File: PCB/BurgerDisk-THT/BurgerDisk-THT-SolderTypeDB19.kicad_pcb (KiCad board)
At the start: 2 copper layers, 93.7 x 67.6 mm, 18 parts, among them J1 Daisy port in, J2 MicroSD module, J3 UART, J4 Daisy port out, U1 PC817

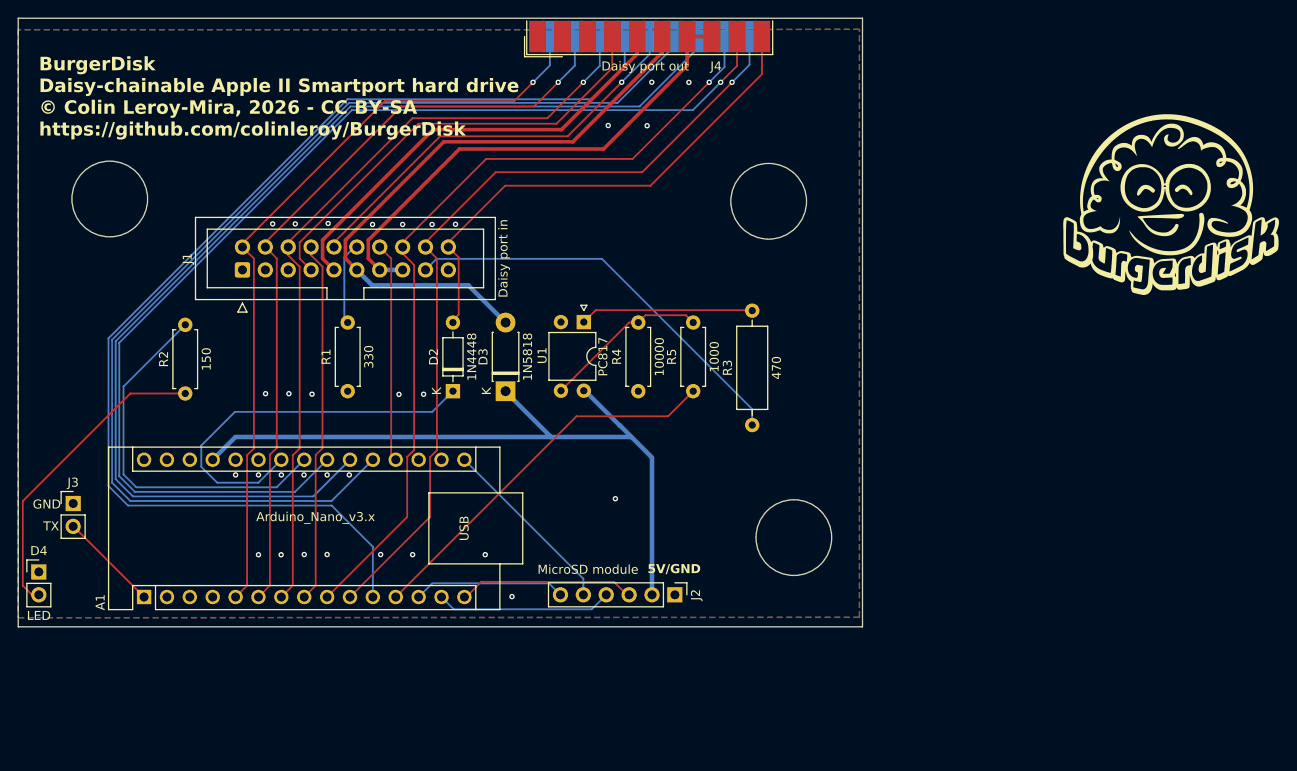
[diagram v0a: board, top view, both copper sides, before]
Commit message: Make PCBs closer to one another
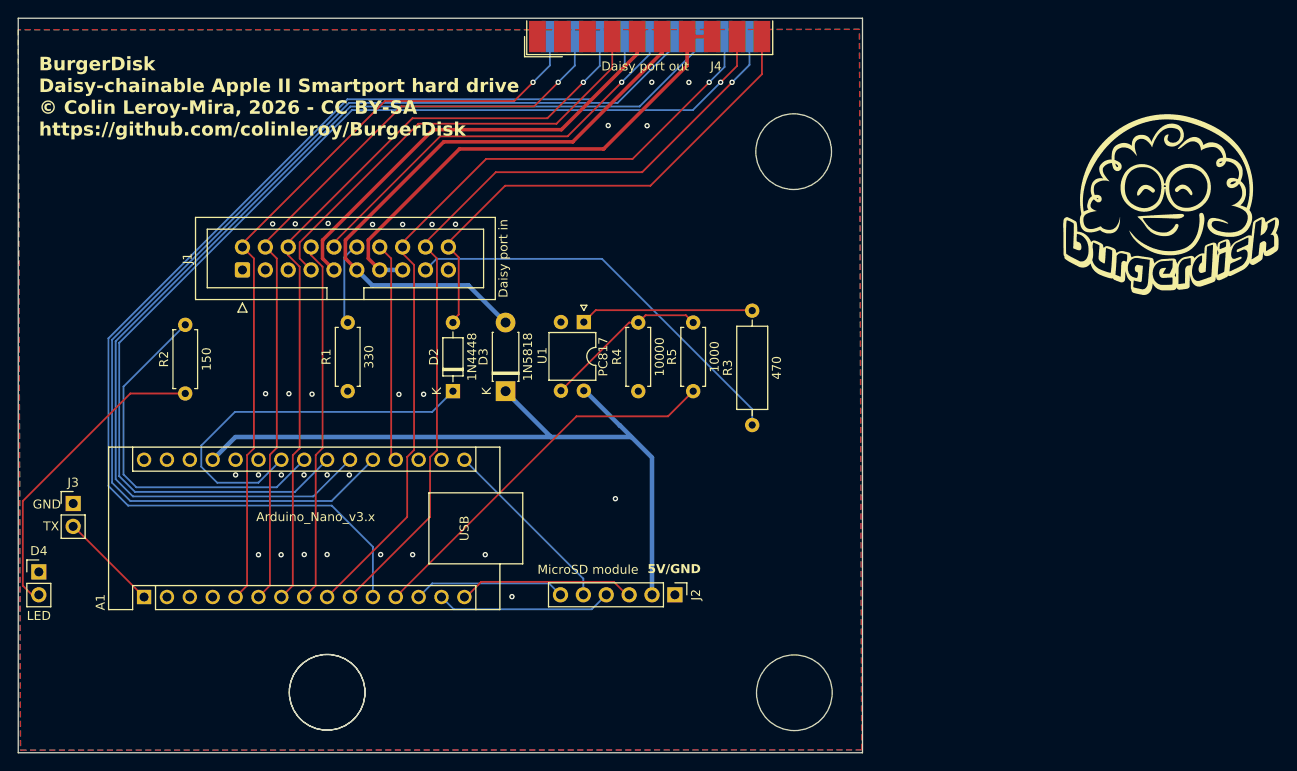
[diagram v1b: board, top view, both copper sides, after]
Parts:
- removed the REF** at (154.2, 64.0)
- removed the REF** at (157.0, 101.3)
- removed the REF** at (81.0, 63.8)
- added ?: , , F.Cu at (105.2, 118.5)
- added REF**: MountingHole_8.4mm_M8, MountingHole:MountingHole_8.4mm_M8, F.Cu at (105.2, 118.5)
- added REF**: MountingHole_8.4mm_M8, MountingHole:MountingHole_8.4mm_M8, F.Cu at (157.0, 58.5)
- added REF**: MountingHole_8.4mm_M8, MountingHole:MountingHole_8.4mm_M8, F.Cu at (157.0, 118.6)
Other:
- board size 93.7 x 67.6 mm -> 93.7 x 81.5 mm

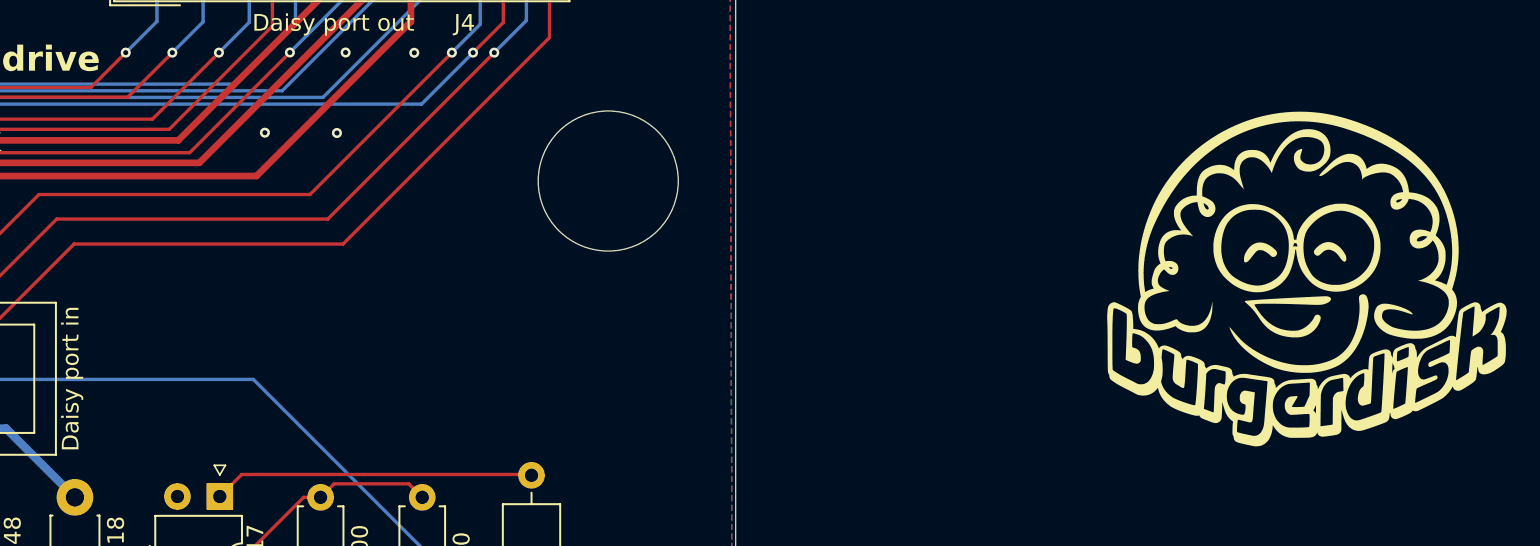
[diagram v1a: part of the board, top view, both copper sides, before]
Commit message: Put the logo back on the PCB
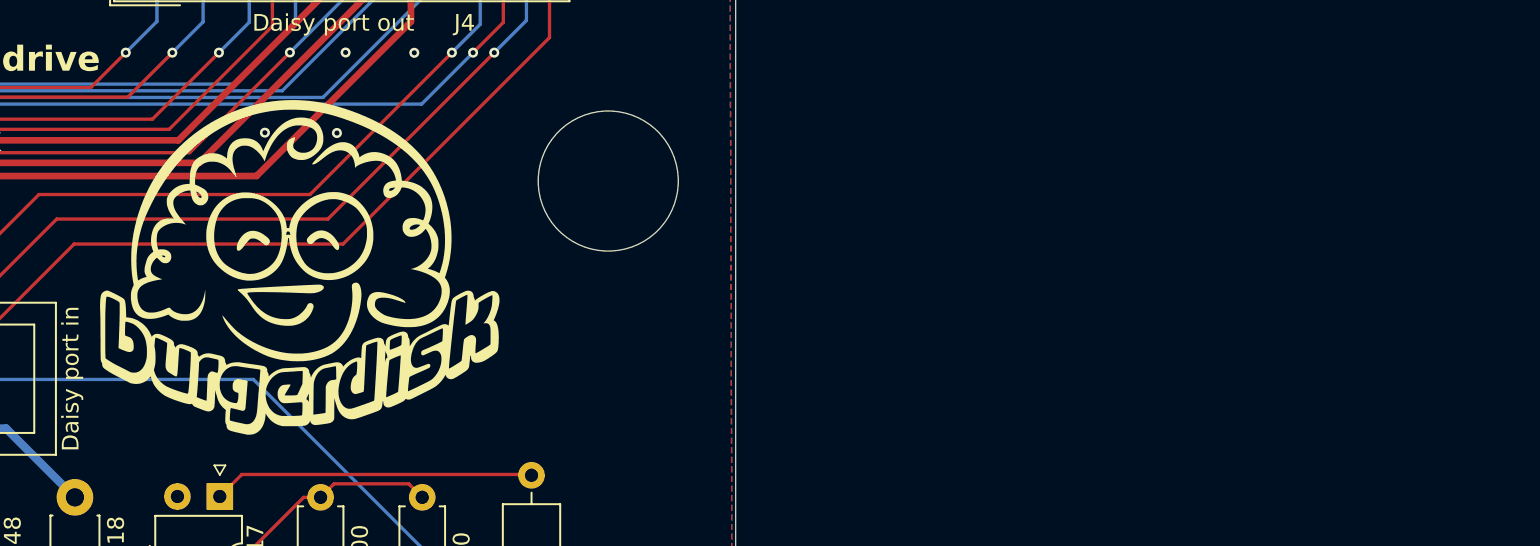
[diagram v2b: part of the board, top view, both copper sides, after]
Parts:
- moved G*** 60.4 mm to (138.4, 63.8)
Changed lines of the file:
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@@
 	(footprint "LOGO"
 		(layer "F.Cu")
-		(at 198.829486 64.451489)
+		(at 138.43 63.754)
 		(property "Reference" "G***"
 			(at 0 0 0)
